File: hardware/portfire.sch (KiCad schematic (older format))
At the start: 56 parts, among them IC101 STM32F407VGT6TR, IC102 TPS62152, IC103 25AA02E48, IC104 ADP3335, IC105 SNx5176B, P101 SWD_TC, P102 AUX_BUS_RX, P103 AUX_BUS_RX, X101 PART, X102 PART, X103 PART, X104 PART, Y101 26M

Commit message: Lots of placement/routing
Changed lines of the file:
@@
 	1    0    0    -1
 $EndComp
+Text Label 3700 4150 0    60   ~ 0
+STATUS
+Text Label 3700 4250 0    60   ~ 0
+ERROR
+Text Label 9350 1650 2    60   ~ 0
+LINK
 $EndSCHEMATC

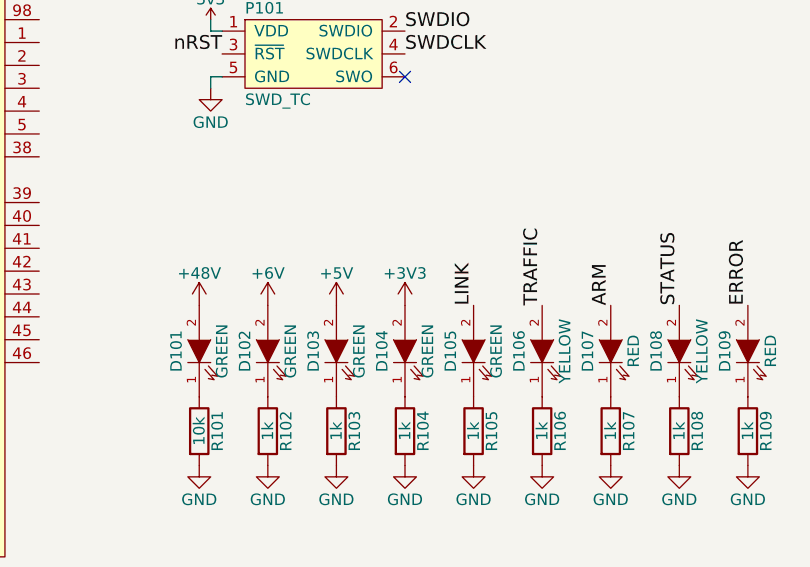
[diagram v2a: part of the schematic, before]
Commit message: Placed uc, routed RMII
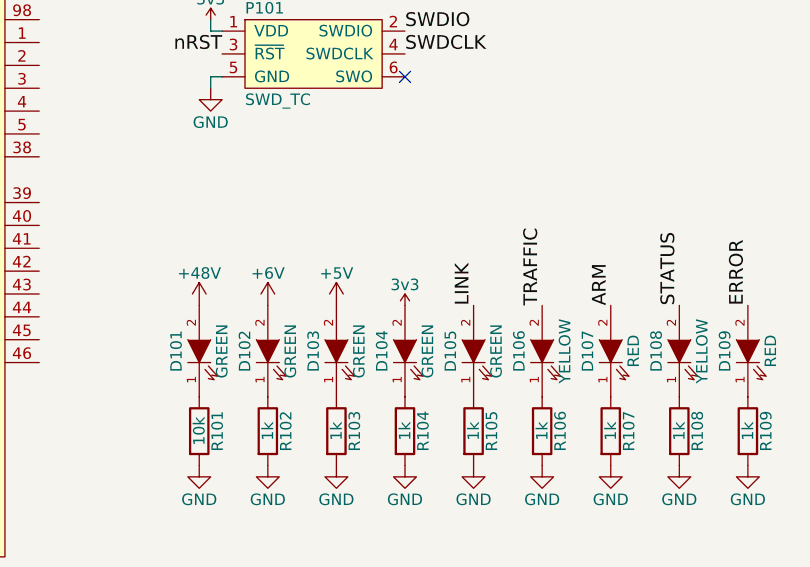
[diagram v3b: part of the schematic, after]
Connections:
- net +3V3 is gone; now on net 3v3: D104.2 (A)

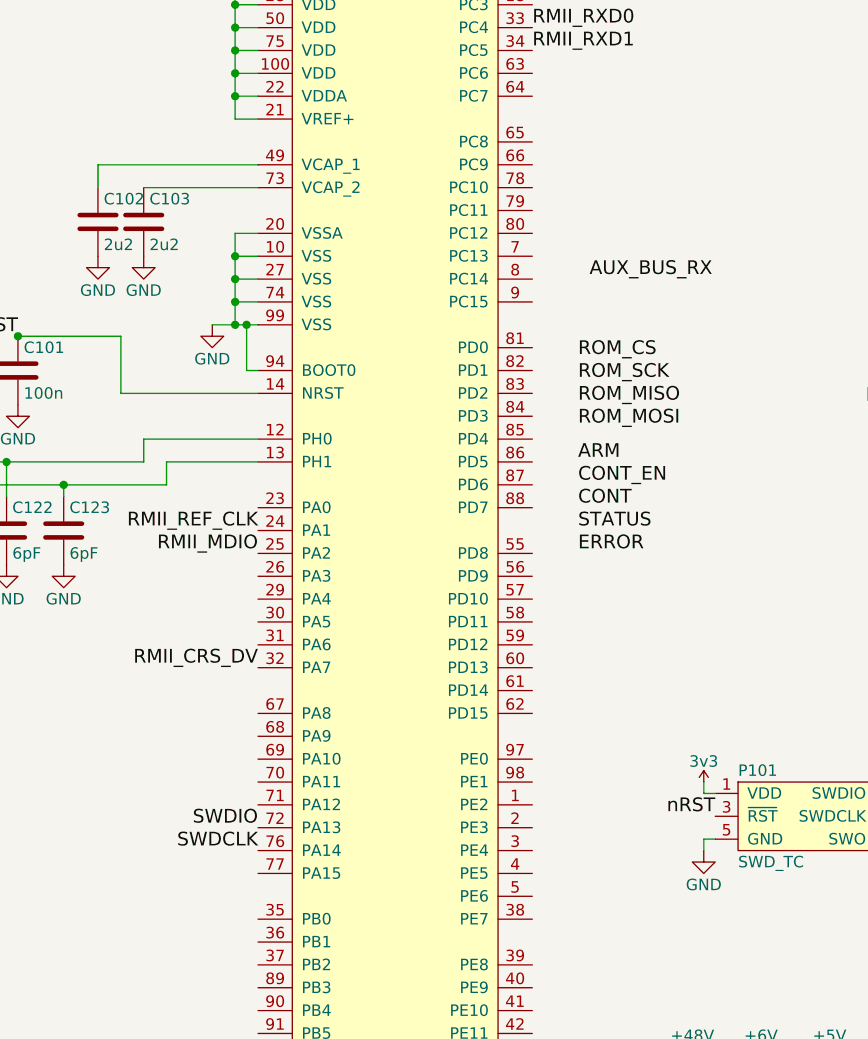
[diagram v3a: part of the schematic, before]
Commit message: Routed ROM
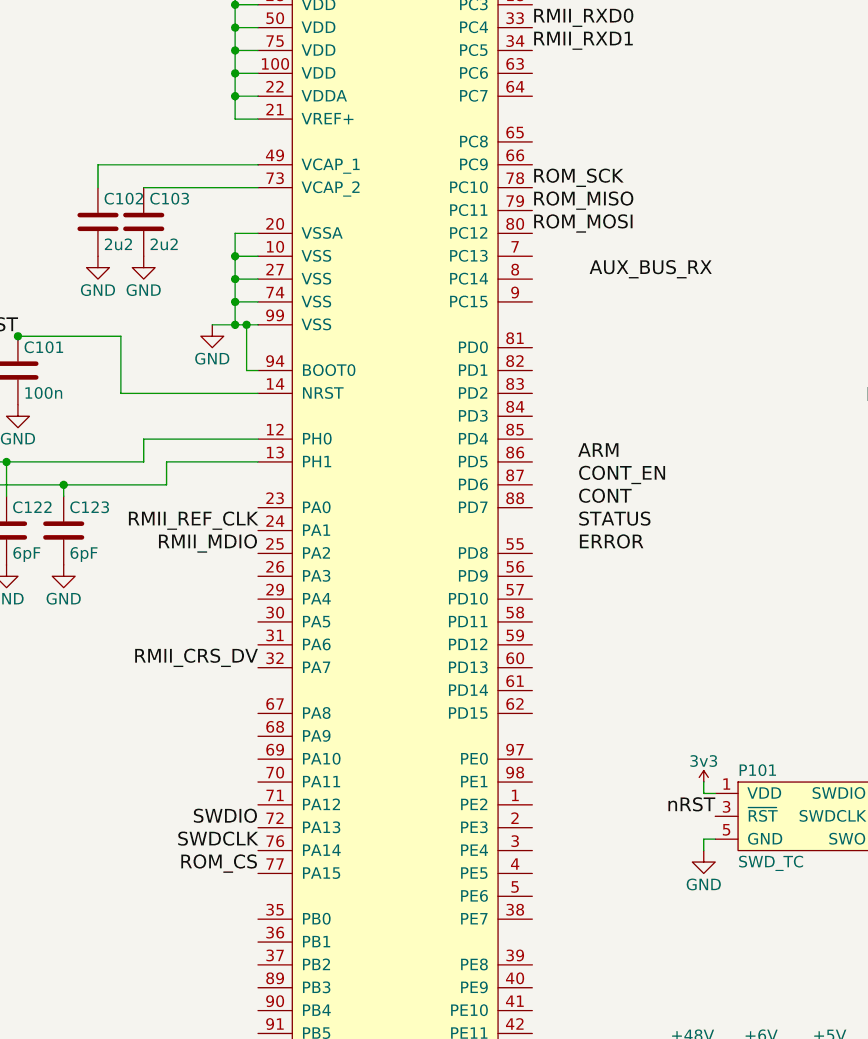
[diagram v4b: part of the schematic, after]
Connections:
- net ROM_CS: now also IC101.77 (PA15)
- net ROM_MISO: now also IC101.79 (PC11)
- net ROM_MOSI: now also IC101.80 (PC12)
- net ROM_SCK: now also IC101.78 (PC10)
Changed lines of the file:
@@
 Text Label 8150 5700 0    60   ~ 0
 ROM_MOSI
-Text Label 3700 3400 0    60   ~ 0
+Text Label 2300 5650 2    60   ~ 0
 ROM_CS
-Text Label 3700 3500 0    60   ~ 0
+Text Label 3500 2650 0    60   ~ 0
 ROM_SCK
-Text Label 3700 3600 0    60   ~ 0
+Text Label 3500 2750 0    60   ~ 0
 ROM_MISO
-Text Label 3700 3700 0    60   ~ 0
+Text Label 3500 2850 0    60   ~ 0
 ROM_MOSI
 $Comp

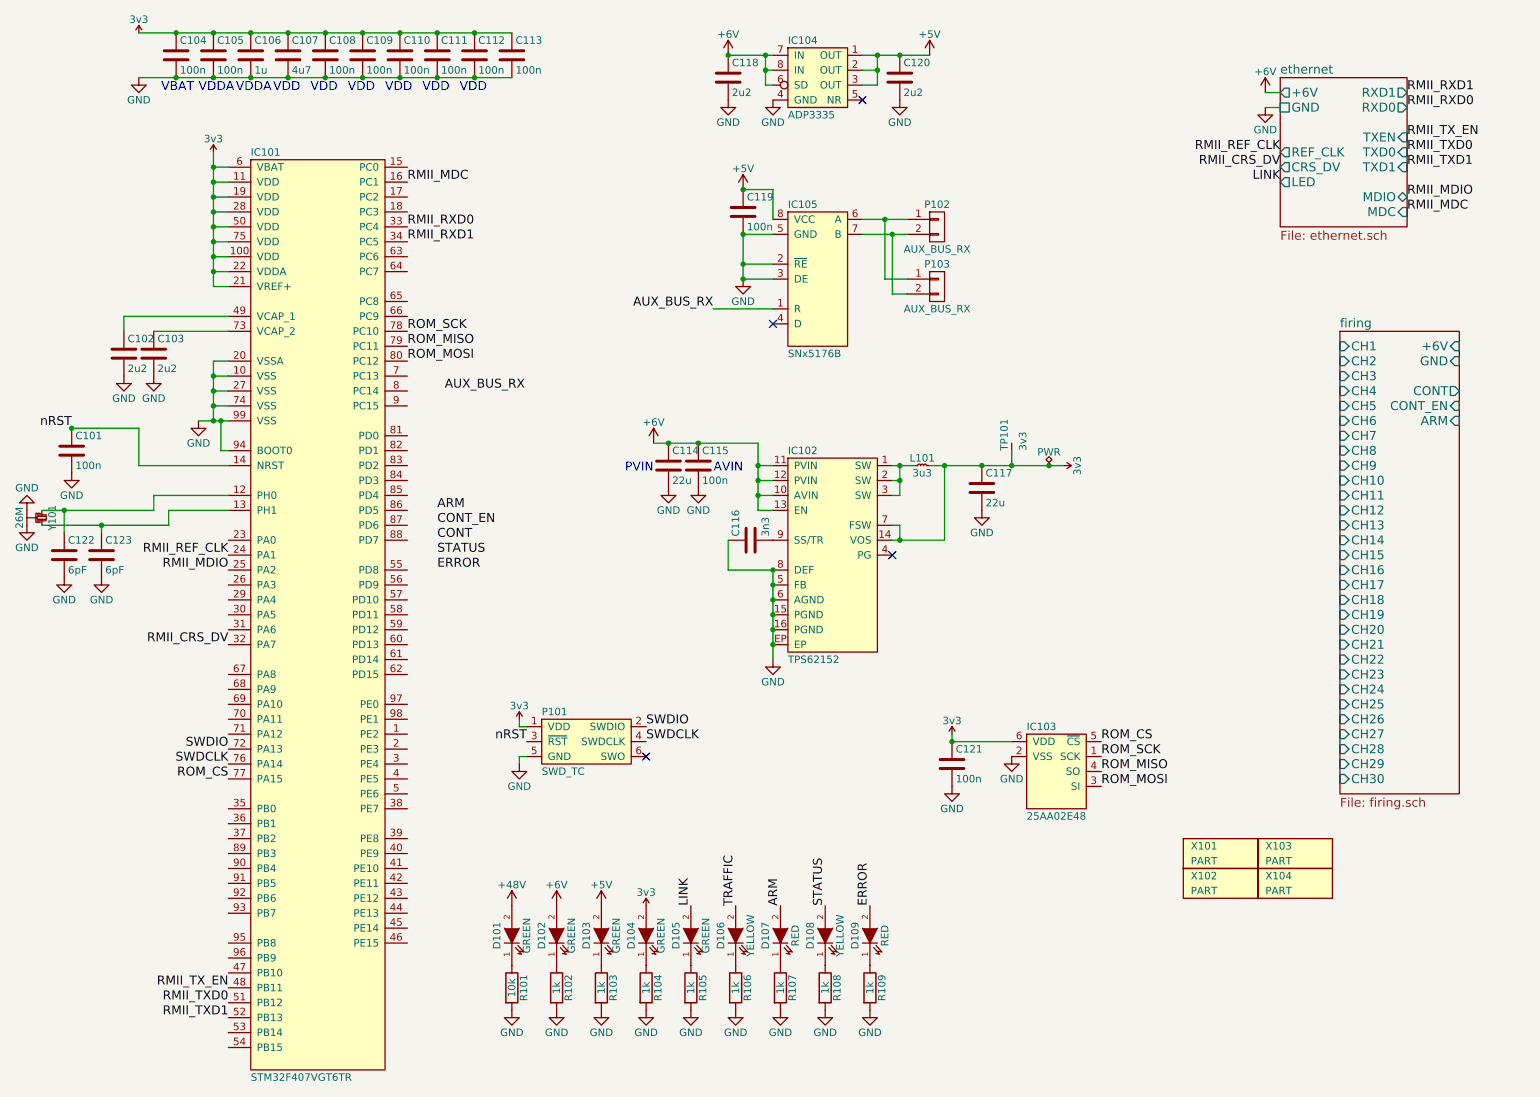
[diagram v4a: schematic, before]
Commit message: Routed cont, arm, LEDs
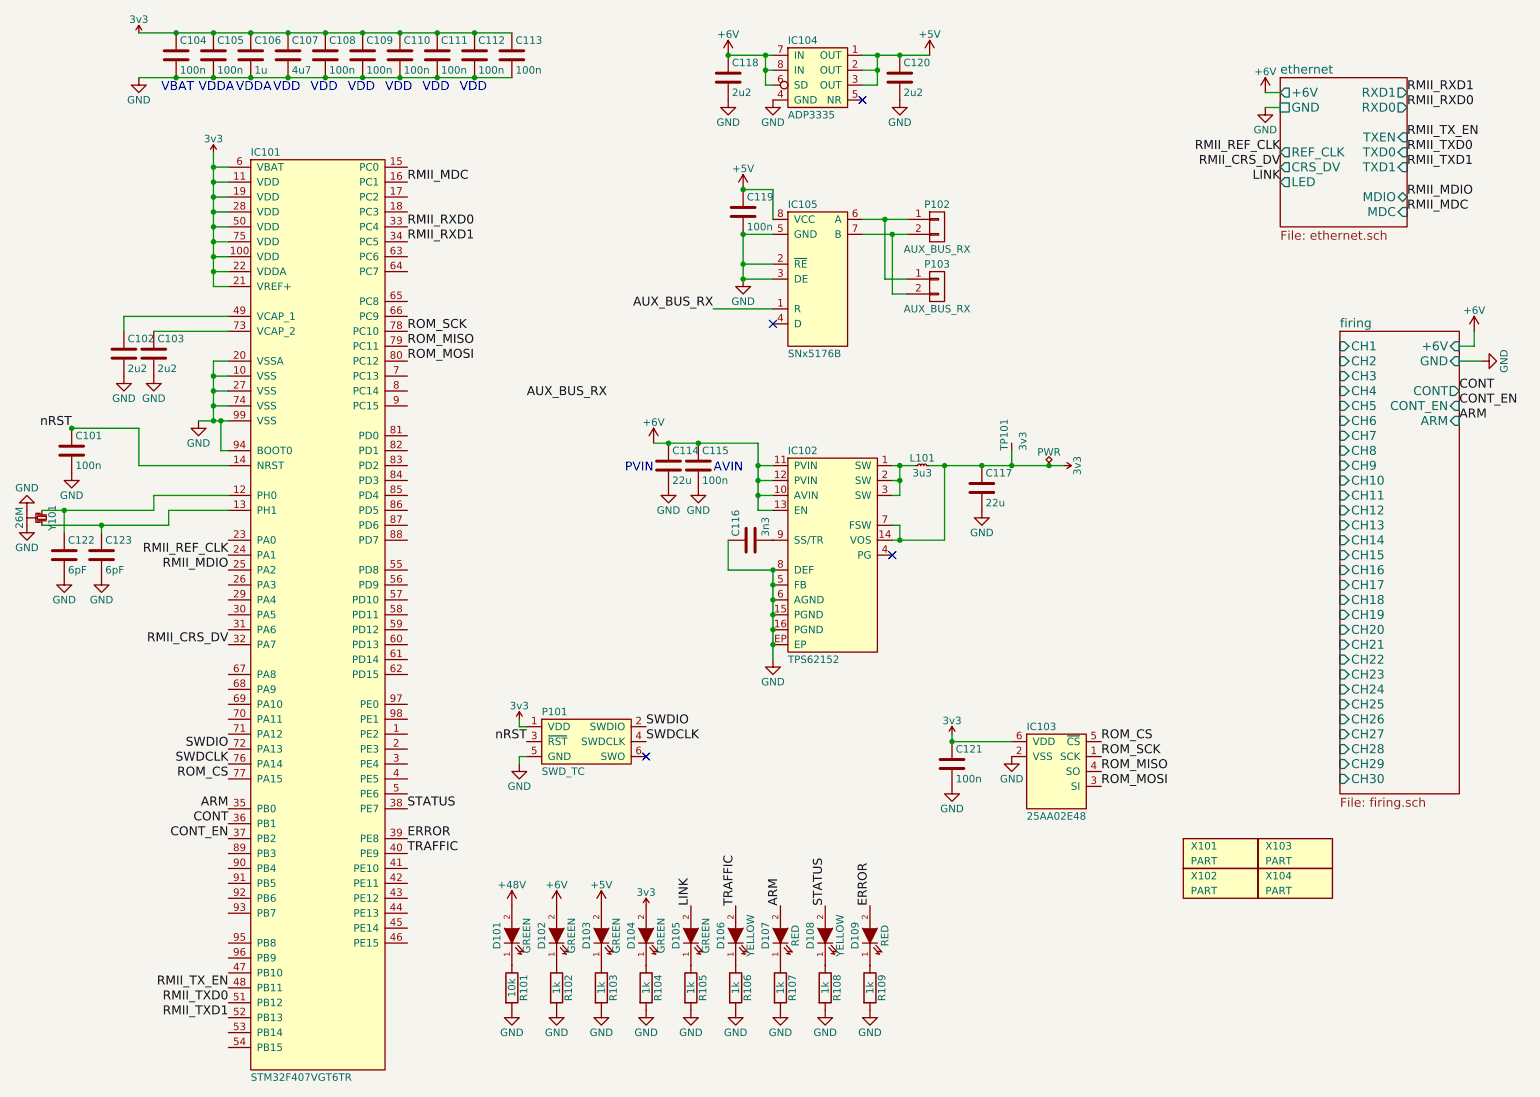
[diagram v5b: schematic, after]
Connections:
- net ARM: now also IC101.35 (PB0)
- net CONT: now also IC101.36 (PB1)
- net CONT_EN: now also IC101.37 (PB2)
- net ERROR: now also IC101.39 (PE8)
- net STATUS: now also IC101.38 (PE7)
- net TRAFFIC: now also IC101.40 (PE9)

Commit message: Routed firing channels
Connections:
- net AUX_BUS_RX: now also IC101.26 (PA3)
- net CH7: now reaches IC101.41 (PE10)
- net CH6: now reaches IC101.42 (PE11)
- net CH5: now reaches IC101.43 (PE12)
- net CH4: now reaches IC101.44 (PE13)
- net CH3: now reaches IC101.45 (PE14)
- net CH2: now reaches IC101.46 (PE15)
- net CH1: now reaches IC101.47 (PB10)
- net CH8: now reaches IC101.53 (PB14)
- net CH9: now reaches IC101.54 (PB15)
- net CH10: now reaches IC101.55 (PD8)
- net CH11: now reaches IC101.56 (PD9)
- net CH12: now reaches IC101.58 (PD11)
- net CH13: now reaches IC101.59 (PD12)
- net CH14: now reaches IC101.60 (PD13)
- net CH15: now reaches IC101.61 (PD14)
- net CH16: now reaches IC101.63 (PC6)
- net CH17: now reaches IC101.64 (PC7)
- net CH18: now reaches IC101.65 (PC8)
- net CH19: now reaches IC101.67 (PA8)
- net CH20: now reaches IC101.68 (PA9)
- net CH21: now reaches IC101.69 (PA10)
- net CH22: now reaches IC101.89 (PB3)
- net CH23: now reaches IC101.90 (PB4)
- net CH24: now reaches IC101.91 (PB5)
- net CH25: now reaches IC101.92 (PB6)
- net CH26: now reaches IC101.93 (PB7)
- net CH30: now reaches IC101.95 (PB8)
- net CH29: now reaches IC101.96 (PB9)
- net CH28: now reaches IC101.97 (PE0)
- net CH27: now reaches IC101.98 (PE1)
- no-connect marks 4 -> 5
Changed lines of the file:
@@
 $EndDescr
-$Comp
-L STM32F4xxVxTx IC101
-U 1 1 57E9C730
-P 2900 4550
-F 0 "IC101" H 2450 7650 50  0000 L CNN
-F 1 "STM32F407VGT6TR" H 2450 1450 50  0000 L CNN
-F 2 "agg:LQFP-100" H 2450 1350 50  0001 L CNN
-F 3 "http://www.st.com/st-web-ui/static/active/en/resource/technical/document/datasheet/DM00037051.pdf" H 2450 1250 50  0001 L CNN
-F 4 "2333297" H 2450 1150 50  0001 L CNN "Farnell"
-	1    2900 4550
-	1    0    0    -1
-$EndComp
 $Comp
 L 25AA02E48 IC103
@@
 	1    0    0    -1
 $EndComp
-Text Label 4300 3100 0    60   ~ 0
+Text Label 2300 4350 2    60   ~ 0
 AUX_BUS_RX
 $Comp
@@
 Text Label 3500 6150 0    60   ~ 0
 TRAFFIC
+Text Label 2300 6950 2    60   ~ 0
+CH1
+Text Label 3500 6750 0    60   ~ 0
+CH2
+Text Label 3500 6650 0    60   ~ 0
+CH3
+Text Label 3500 6550 0    60   ~ 0
+CH4
+Text Label 3500 6450 0    60   ~ 0
+CH5
+Text Label 3500 6350 0    60   ~ 0
+CH6
+Text Label 9750 2750 2    60   ~ 0
+CH1
+Text Label 9750 2850 2    60   ~ 0
+CH2
+Text Label 9750 2950 2    60   ~ 0
+CH3
+Text Label 9750 3050 2    60   ~ 0
+CH4
+Text Label 9750 3150 2    60   ~ 0
+CH5
+Text Label 9750 3250 2    60   ~ 0
+CH6
+Text Label 3500 6250 0    60   ~ 0
+CH7
+Text Label 9750 3350 2    60   ~ 0
+CH7
+Text Label 2300 7350 2    60   ~ 0
+CH8
+Text Label 2300 7450 2    60   ~ 0
+CH9
+Text Label 9750 3450 2    60   ~ 0
+CH8
+Text Label 9750 3550 2    60   ~ 0
+CH9
+Text Label 3500 4250 0    60   ~ 0
+CH10
+Text Label 3500 4350 0    60   ~ 0
+CH11
+Text Label 3500 4550 0    60   ~ 0
+CH12
+Text Label 3500 4650 0    60   ~ 0
+CH13
+Text Label 3500 4750 0    60   ~ 0
+CH14
+Text Label 3500 4850 0    60   ~ 0
+CH15
+Text Label 9750 4150 2    60   ~ 0
+CH15
+Text Label 9750 4050 2    60   ~ 0
+CH14
+Text Label 9750 3950 2    60   ~ 0
+CH13
+Text Label 9750 3850 2    60   ~ 0
+CH12
+Text Label 9750 3750 2    60   ~ 0
+CH11
+Text Label 9750 3650 2    60   ~ 0
+CH10
+NoConn ~ 3500 4450
+Text Label 3500 2150 0    60   ~ 0
+CH16
+Text Label 3500 2250 0    60   ~ 0
+CH17
+Text Label 9750 4250 2    60   ~ 0
+CH16
+Text Label 9750 4350 2    60   ~ 0
+CH17
+Text Label 9750 4450 2    60   ~ 0
+CH18
+Text Label 3500 2450 0    60   ~ 0
+CH18
+Text Label 2300 4950 2    60   ~ 0
+CH19
+Text Label 9750 4550 2    60   ~ 0
+CH19
+Text Label 9750 4650 2    60   ~ 0
+CH20
+Text Label 9750 4750 2    60   ~ 0
+CH21
+Text Label 9750 4850 2    60   ~ 0
+CH22
+Text Label 9750 4950 2    60   ~ 0
+CH23
+Text Label 9750 5050 2    60   ~ 0
+CH24
+Text Label 9750 5150 2    60   ~ 0
+CH25
+Text Label 9750 5250 2    60   ~ 0
+CH26
+Text Label 9750 5350 2    60   ~ 0
+CH27
+Text Label 9750 5450 2    60   ~ 0
+CH28
+Text Label 9750 5550 2    60   ~ 0
+CH29
+Text Label 9750 5650 2    60   ~ 0
+CH30
+Text Label 2300 5050 2    60   ~ 0
+CH20
+Text Label 2300 5150 2    60   ~ 0
+CH21
+$Comp
+L STM32F4xxVxTx IC101
+U 1 1 57E9C730
+P 2900 4550
+F 0 "IC101" H 2450 7650 50  0000 L CNN
+F 1 "STM32F407VGT6TR" H 2450 1450 50  0000 L CNN
+F 2 "agg:LQFP-100" H 2450 1350 50  0001 L CNN
+F 3 "http://www.st.com/st-web-ui/static/active/en/resource/technical/document/datasheet/DM00037051.pdf" H 2450 1250 50  0001 L CNN
+F 4 "2333297" H 2450 1150 50  0001 L CNN "Farnell"
+	1    2900 4550
+	1    0    0    -1
+$EndComp
+Text Label 2300 6750 2    60   ~ 0
+CH30
+Text Label 2300 6850 2    60   ~ 0
+CH29
+Text Label 3500 5150 0    60   ~ 0
+CH28
+Text Label 3500 5250 0    60   ~ 0
+CH27
+Text Label 2300 6550 2    60   ~ 0
+CH26
+Text Label 2300 6450 2    60   ~ 0
+CH25
+Text Label 2300 6350 2    60   ~ 0
+CH24
+Text Label 2300 6250 2    60   ~ 0
+CH23
+Text Label 2300 6150 2    60   ~ 0
+CH22
 $EndSCHEMATC
